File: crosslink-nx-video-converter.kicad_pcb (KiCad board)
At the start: 2 copper layers, 105.7 x 60 mm, 37 parts, among them J1 DC_SOCKET, J2 031-70526-21, J3 031-70526-21, J4 WE_68715014522_ONE-SIDE, J5 WE_68715014522_ONE-SIDE, J6 FTSH-105-01-F-DV-K, J7 FTSH-105-01-L-DV-K, J8 2X05, SW1 SW_DIP_x06, U1 NCV51200MNTXG, U10 GS2971A, U11 LIFCL-40-9BG256C, U12 SC18IS602BIPW, U13 W25Q32JVSSIQ, U2 AP62301WU-7, U3 AP62301WU-7, U4 AP62301WU-7, U5 AP7330-W5-7, U6 AP7330-W5-7, U7 AP7330-W5-7, U8 MT41K128M16JT-125_K, U9 GS2988, Y1 ABM7_27.000MH_D2Y_T, Y2 OSC40M-3.3_S5

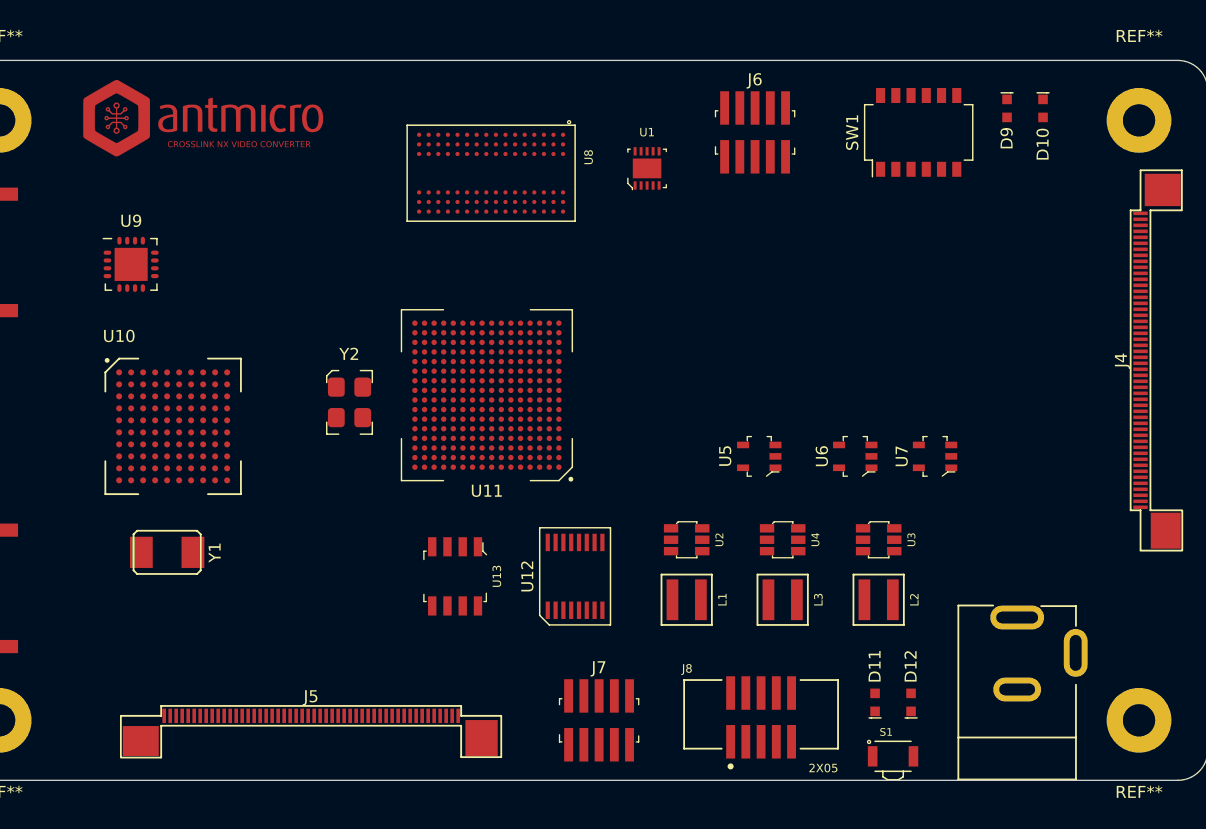
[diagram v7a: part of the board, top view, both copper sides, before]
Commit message: Modified power indicator and connected unused pins
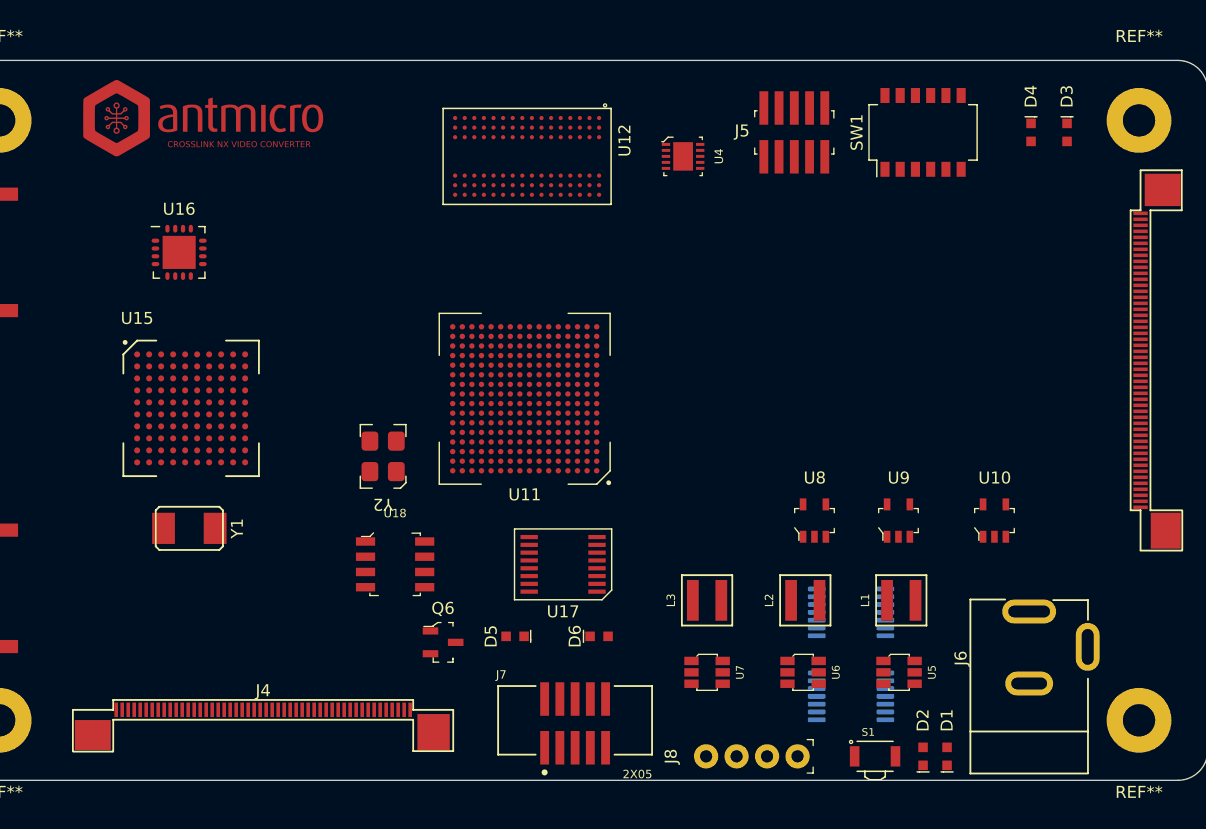
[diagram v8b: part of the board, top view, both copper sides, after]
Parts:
- removed D10, D11, D9: LTST-C190GKT, crosslink-nx-video-converter-footprints:LED_0603
- removed D12: LTST-C190KRKT, crosslink-nx-video-converter-footprints:LED_0603
- removed U1: NCV51200MNTXG, crosslink-nx-video-converter-footprints:DFN-10-1EP_3x3mm
- removed U13: W25Q32JVSSIQ, crosslink-nx-video-converter-footprints:SOIC-8_W5.3mm
- added D1: LTST-C190GKT, crosslink-nx-video-converter-footprints:LED_0603, F.Cu at (159.0, 113.0)
- added D2: LTST-C190GKT, crosslink-nx-video-converter-footprints:LED_0603, F.Cu at (157.0, 113.0)
- added D3: LTST-C190GKT, crosslink-nx-video-converter-footprints:LED_0603, F.Cu at (169.0, 61.0)
- added D4: LTST-C190GKT, crosslink-nx-video-converter-footprints:LED_0603, F.Cu at (166.0, 61.0)
- added D5: LTST-C190GKT, crosslink-nx-video-converter-footprints:LED_0603, F.Cu at (123.0, 103.0)
- added D6: LTST-C190KRKT, crosslink-nx-video-converter-footprints:LED_0603, F.Cu at (130.0, 103.0)
- added Q6: 2N7002, crosslink-nx-video-converter-footprints:SOT-23-3, F.Cu at (117.0, 103.5)
- added U15: GS2971A, crosslink-nx-video-converter-footprints:BGA100_11x11mm, F.Cu at (96.0, 84.0)
- added U16: GS2988, crosslink-nx-video-converter-footprints:QFN-16_EP_4x4_Pitch0.65mm, F.Cu at (95.0, 71.0)
- added U17: SC18IS602BIPW, crosslink-nx-video-converter-footprints:SC18IS602B, F.Cu at (127.0, 97.0)
- added U18: W25Q32JVSSIQ, crosslink-nx-video-converter-footprints:SOIC-8_W5.3mm, F.Cu at (113.0, 97.0)
- J5: value WE_68715014522_ONE-SIDE -> FTSH-105-01-F-DV-K; footprint crosslink-nx-video-converter-footprints:WE_68715014522_ONE-SIDE -> crosslink-nx-video-converter-footprints:PinHeader_2x5_P1.27_SMD
- J6: value FTSH-105-01-F-DV-K -> WE_68715014522_ONE-SIDE; footprint crosslink-nx-video-converter-footprints:PinHeader_2x5_P1.27_SMD -> crosslink-nx-video-converter-footprints:WE_68715014522_ONE-SIDE
- J7: value FTSH-105-01-L-DV-K -> 2X05; footprint crosslink-nx-video-converter-footprints:PinHeader_2x5_P1.27_SMD -> crosslink-nx-video-converter-footprints:SHF-105-01-X-D-SM
- J8: value 2X05 -> 61300411121; footprint crosslink-nx-video-converter-footprints:SHF-105-01-X-D-SM -> antmicro-footprints:PinHeader_1x4_P2.54mm_Drill1.02mm
- U10: value GS2971A -> AP7330-W5-7; footprint crosslink-nx-video-converter-footprints:BGA100_11x11mm -> crosslink-nx-video-converter-footprints:SOT-23-5
- U11: footprint crosslink-nx-video-converter-footprints:BGA-256_16x16_14.0x14.0mm -> antmicro-footprints:BGA-256_16x16_14.0x14.0mm
- U12: value SC18IS602BIPW -> MT41K128M16JT-125_K; footprint crosslink-nx-video-converter-footprints:SC18IS602B -> crosslink-nx-video-converter-footprints:BGA80P96C6X16_800X1400X110
- U2, U3: value AP62301WU-7 -> LM339; footprint crosslink-nx-video-converter-footprints:TSOT23-6 -> antmicro-footprints:TSSOP-14_4.4x5mm_P0.65mm; moved to B.Cu
- U4: value AP62301WU-7 -> NCV51200MNTXG; footprint crosslink-nx-video-converter-footprints:TSOT23-6 -> crosslink-nx-video-converter-footprints:DFN-10-1EP_3x3mm
- U5, U6, U7: value AP7330-W5-7 -> AP62301WU-7; footprint crosslink-nx-video-converter-footprints:SOT-23-5 -> crosslink-nx-video-converter-footprints:TSOT23-6
- U8: value MT41K128M16JT-125_K -> AP7330-W5-7; footprint crosslink-nx-video-converter-footprints:BGA80P96C6X16_800X1400X110 -> crosslink-nx-video-converter-footprints:SOT-23-5
- U9: value GS2988 -> AP7330-W5-7; footprint crosslink-nx-video-converter-footprints:QFN-16_EP_4x4_Pitch0.65mm -> crosslink-nx-video-converter-footprints:SOT-23-5
- moved J4 77.9 mm to (102.0, 108.5), turned to 0 degrees
- moved U10 68.9 mm to (162.9, 93.3)
- moved U9 67.4 mm to (154.9, 93.3)
- moved J5 62.7 mm to (146.3, 61.0), turned to 180 degrees
- moved U8 39.6 mm to (147.9, 93.3), turned to 0 degrees
- moved J6 36.8 mm to (174.5, 80.0), turned to 90 degrees
- moved U12 35.2 mm to (124.0, 63.0), turned to -90 degrees
- moved U4 33.0 mm to (137.0, 63.0)
- moved U7 26.2 mm to (139.0, 106.0), turned to -90 degrees
- moved U5 21.4 mm to (155.0, 106.0), turned to -90 degrees
- moved U6 18.5 mm to (147.0, 106.0), turned to -90 degrees
- moved L1 17.9 mm to (155.2, 100.0), turned to 180 degrees
- moved U2 15.0 mm to (151.0, 101.0), turned to 0 degrees
- moved U3 13.3 mm to (151.0, 108.0), turned to 0 degrees
- moved L3 6.30 mm to (139.0, 100.0), turned to 180 degrees
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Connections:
- net /FPGA/40MHz_3V3 renamed 40MHz_3V3
- net /FPGA/JTAG_EN renamed JTAG_EN
- net /FPGA/TCK renamed TCK
- net /FPGA/TDI renamed TDI
- net /FPGA/TDO renamed TDO
- net /FPGA/TMS renamed TMS
- net FCC1_SCL1 renamed /Peripherals/FCC1_SCL1
- net FCC1_SCL2 renamed /Peripherals/FCC1_SCL2
- net FCC1_SDA1 renamed /Peripherals/FCC1_SDA1
- net FCC1_SDA2 renamed /Peripherals/FCC1_SDA2
- net FFC1_RESET renamed /Peripherals/FFC1_RESET
- net FFC1_VSYNC0 renamed /Peripherals/FFC1_VSYNC0
- net FFC1_VSYNC1 renamed /Peripherals/FFC1_VSYNC1
- net MIPI0_CLK_N renamed /Peripherals/MIPI0_CLK_N
- net MIPI0_CLK_P renamed /Peripherals/MIPI0_CLK_P
- net MIPI0_D0_N renamed /Peripherals/MIPI0_D0_N
- net MIPI0_D0_P renamed /Peripherals/MIPI0_D0_P
- net MIPI0_D1_N renamed /Peripherals/MIPI0_D1_N
- net MIPI0_D1_P renamed /Peripherals/MIPI0_D1_P
- net MIPI0_D2_N renamed /Peripherals/MIPI0_D2_N
- net MIPI0_D2_P renamed /Peripherals/MIPI0_D2_P
- net MIPI0_D3_N renamed /Peripherals/MIPI0_D3_N
- net MIPI0_D3_P renamed /Peripherals/MIPI0_D3_P
- J4 pad 19: MIPI1_D3_N -> /Peripherals/MIPI2_D3_N
- J4 pad 20: MIPI1_D3_P -> /Peripherals/MIPI2_D3_P
- J4 pad 21: MIPI1_D2_N -> /Peripherals/MIPI2_D2_N
- J4 pad 22: MIPI1_D2_P -> /Peripherals/MIPI2_D2_P
- J4 pad 23: MIPI1_D1_N -> /Peripherals/MIPI2_D1_N
- J4 pad 24: MIPI1_D1_P -> /Peripherals/MIPI2_D1_P
- J4 pad 25: MIPI1_D0_N -> /Peripherals/MIPI2_D0_N
- J4 pad 26: MIPI1_D0_P -> /Peripherals/MIPI2_D0_P
- J4 pad 28: MIPI1_CLK_N -> /Peripherals/MIPI2_CLK_N
- J4 pad 29: MIPI1_CLK_P -> /Peripherals/MIPI2_CLK_P
- J5 pad 1: unconnected-(J5-Pad1) -> AUDIO_ACLK
- J5 pad 10: unconnected-(J5-Pad10) -> AUDIO_MCLK
- J5 pad 2: unconnected-(J5-Pad2) -> AUDIO_ACLK
- J5 pad 3: unconnected-(J5-Pad3) -> AUDIO_WCLK
- J5 pad 4: unconnected-(J5-Pad4) -> AUDIO_WCLK
- J5 pad 5: unconnected-(J5-Pad5) -> AUDIO_OUT_CH1_2
- J5 pad 6: unconnected-(J5-Pad6) -> AUDIO_OUT_CH5_6
- J5 pad 7: unconnected-(J5-Pad7) -> AUDIO_OUT_CH3_4
- J5 pad 8: unconnected-(J5-Pad8) -> AUDIO_OUT_CH7_8
- J6 pad 1: AUDIO_ACLK -> unconnected-(J6-Pad1)
- J6 pad 10: AUDIO_MCLK -> unconnected-(J6-Pad10)
- J6 pad 2: AUDIO_ACLK -> unconnected-(J6-Pad2)
- J6 pad 3: AUDIO_WCLK -> unconnected-(J6-Pad3)
- J6 pad 4: AUDIO_WCLK -> unconnected-(J6-Pad4)
- J6 pad 5: AUDIO_OUT_CH1_2 -> unconnected-(J6-Pad5)
- J6 pad 6: AUDIO_OUT_CH5_6 -> unconnected-(J6-Pad6)
- J6 pad 7: AUDIO_OUT_CH3_4 -> unconnected-(J6-Pad7)
- J6 pad 8: AUDIO_OUT_CH7_8 -> unconnected-(J6-Pad8)
- J7 pad 1: unconnected-(J7-Pad1) -> +3V3
- J7 pad 10: GND -> Net-(J7-Pad10)
- J7 pad 2: FCC2_SDA1 -> Net-(J7-Pad2)
- J7 pad 3: /FPGA/SPI_CLK_SOFT -> GND
- J7 pad 4: FCC2_SCL1 -> Net-(J7-Pad4)
- J7 pad 5: /FPGA/MOSI_SOFT -> GND
- J7 pad 6: GND -> Net-(J7-Pad6)
- J7 pad 7: /FPGA/MISO_SOFT -> unconnected-(J7-Pad7)
- J7 pad 8: /FPGA/PROGRAMN_SOFT -> Net-(J7-Pad8)
- J7 pad 9: /FPGA/~{FLASH_CS_SOFT} -> GND
- J8 pad 1: +3V3 -> GND
- J8 pad 2: Net-(J8-Pad2) -> SCL
- J8 pad 3: GND -> SDA
- J8 pad 4: Net-(J8-Pad4) -> GND
- L1 pad 1: Net-(C12-Pad2) -> Net-(C14-Pad2)
- L2 pad 1: Net-(C13-Pad2) -> Net-(C15-Pad2)
- L3 pad 1: Net-(C14-Pad2) -> Net-(C16-Pad2)
- U11 pad A3: MIPI1_D2_P -> /Peripherals/MIPI1_D2_P
- U11 pad A4: MIPI1_D0_P -> /Peripherals/MIPI1_D0_P
- U11 pad A5: MIPI1_CLK_P -> /Peripherals/MIPI1_CLK_P
- U11 pad A6: MIPI1_D1_P -> /Peripherals/MIPI1_D1_P
- U11 pad A7: MIPI1_D3_P -> /Peripherals/MIPI1_D3_P
- U11 pad B3: MIPI1_D2_N -> /Peripherals/MIPI1_D2_N
- U11 pad B4: MIPI1_D0_N -> /Peripherals/MIPI1_D0_N
- U11 pad B5: MIPI1_CLK_N -> /Peripherals/MIPI1_CLK_N
- U11 pad B6: MIPI1_D1_N -> /Peripherals/MIPI1_D1_N
- U11 pad B7: MIPI1_D3_N -> /Peripherals/MIPI1_D3_N
- U11 pad D4: RESET_TRST -> /SDI/RESET_TRST
- U11 pad D5: STANDBY -> /SDI/STANDBY
- U11 pad D6: SW_EN -> /SDI/SW_EN
- U11 pad E10: FFC2_VSYNC1 -> /Peripherals/FFC2_VSYNC1
- U11 pad E13: FCC2_SDA2 -> /Peripherals/FCC2_SDA2
- U11 pad E4: ~{CS_TMS} -> /SDI/~{CS_TMS}
- U11 pad E5: SCLK_TCK -> /SDI/SCLK_TCK
- U11 pad E6: TIM_861 -> /SDI/TIM_861
- U11 pad E9: FFC2_RESET -> /Peripherals/FFC2_RESET
- U11 pad F15: FCC2_SCL2 -> /Peripherals/FCC2_SCL2
- U11 pad F4: SDOUT_TDO -> /SDI/SDOUT_TDO
- U11 pad F6: SDIN_TDI -> /SDI/SDIN_TDI
- U11 pad F9: FFC2_VSYNC0 -> /Peripherals/FFC2_VSYNC0
- U11 pad G10: Net-(R70-Pad1) -> SCL
- U11 pad G3: SDI_STAT5 -> /SDI/SDI_STAT5
- U11 pad G4: ~{SDO_DISABLE} -> /SDI/~{SDO_DISABLE}
- U11 pad G6: SDO_EN/DIS -> /SDI/SDO_EN/DIS
- U11 pad G9: Net-(R69-Pad1) -> SDA
- U11 pad H1: SDI_D4 -> /SDI/SDI_D4
- U11 pad H12: DVB_ASI -> /SDI/DVB_ASI
- U11 pad H2: SDI_D5 -> /SDI/SDI_D5
- U11 pad H3: SDI_D3 -> /SDI/SDI_D3
- U11 pad H4: SDI_D2 -> /SDI/SDI_D2
- U11 pad H5: SDI_D1 -> /SDI/SDI_D1
- U11 pad H6: SDI_D0 -> /SDI/SDI_D0
- U11 pad J1: SDI_D7 -> /SDI/SDI_D7
- U11 pad J11: AUDIO_EN/~{DIS} -> /SDI/AUDIO_EN/~{DIS}
- U11 pad J12: IOPROC_EN/~{DIS} -> /SDI/IOPROC_EN/~{DIS}
- U11 pad J15: 20bit/~{10bit} -> /SDI/20bit/~{10bit}
- U11 pad J16: ~{SMPTE_BYPASS} -> /SDI/~{SMPTE_BYPASS}
- U11 pad J2: SDI_D8 -> /SDI/SDI_D8
- U11 pad J5: SDI_D6 -> /SDI/SDI_D6
- U11 pad J6: SDI_PCLK -> /SDI/SDI_PCLK
- U11 pad K1: SDI_D9 -> /SDI/SDI_D9
- U11 pad K11: JTAG/~{HOST} -> /SDI/JTAG/~{HOST}
- U11 pad K12: ~{RC_BYP} -> /SDI/~{RC_BYP}
- U11 pad K2: SDI_D10 -> /SDI/SDI_D10
- U11 pad K3: SDI_D12 -> /SDI/SDI_D12
- U11 pad K4: SDI_D11 -> /SDI/SDI_D11
- U11 pad K5: SDI_D14 -> /SDI/SDI_D14
- U11 pad K6: SDI_D13 -> /SDI/SDI_D13
- U11 pad K7: MIPI2_D3_N -> /Peripherals/MIPI2_D3_N
- U11 pad L1: SDI_D15 -> /SDI/SDI_D15
- U11 pad L10: DDR3_A8 -> /DDR3/DDR3_A8
- U11 pad L11: DDR3_A7 -> /DDR3/DDR3_A7
- U11 pad L12: DDR3_A10 -> /DDR3/DDR3_A10
- U11 pad L2: SDI_D16 -> /SDI/SDI_D16
- U11 pad L3: SDI_STAT2 -> /SDI/SDI_STAT2
- U11 pad L4: SDI_D19 -> /SDI/SDI_D19
- U11 pad L5: SDI_STAT0 -> /SDI/SDI_STAT0
- U11 pad L6: MIPI2_D3_P -> /Peripherals/MIPI2_D3_P
- U11 pad L7: MIPI2_D2_P -> /Peripherals/MIPI2_D2_P
- U11 pad L8: DDR3_BA2 -> /DDR3/DDR3_BA2
- U11 pad L9: ~{DDR3_RAS} -> /DDR3/~{DDR3_RAS}
- U11 pad M1: SDI_D17 -> /SDI/SDI_D17
- U11 pad M10: DDR3_ODT -> /DDR3/DDR3_ODT
- U11 pad M12: DDR3_A6 -> /DDR3/DDR3_A6
- U11 pad M13: DDR3_A9 -> /DDR3/DDR3_A9
- U11 pad M14: DDR3_A3 -> /DDR3/DDR3_A3
- U11 pad M16: DDR3_A11 -> /DDR3/DDR3_A11
- U11 pad M2: SDI_D18 -> /SDI/SDI_D18
- U11 pad M3: SDI_STAT1 -> /SDI/SDI_STAT1
- U11 pad M4: MIPI2_D1_N -> /Peripherals/MIPI2_D1_N
- U11 pad M7: MIPI2_D2_N -> /Peripherals/MIPI2_D2_N
- U11 pad N1: SDI_STAT4 -> /SDI/SDI_STAT4
- U11 pad N10: ~{DDR3_RESET} -> /DDR3/~{DDR3_RESET}
- U11 pad N13: DDR3_A0 -> /DDR3/DDR3_A0
- U11 pad N15: DDR3_A5 -> /DDR3/DDR3_A5
- U11 pad N16: DDR3_A4 -> /DDR3/DDR3_A4
- U11 pad N2: SDI_STAT3 -> /SDI/SDI_STAT3
- U11 pad N3: MIPI2_D0_N -> /Peripherals/MIPI2_D0_N
- U11 pad N4: MIPI2_D1_P -> /Peripherals/MIPI2_D1_P
- U11 pad N8: ~{DDR3_CAS} -> /DDR3/~{DDR3_CAS}
- U11 pad N9: ~{DDR3_WE} -> /DDR3/~{DDR3_WE}
- U11 pad P1: MIPI2_CLK_P -> /Peripherals/MIPI2_CLK_P
- U11 pad P15: DDR3_A1 -> /DDR3/DDR3_A1
- U11 pad P16: DDR3_A2 -> /DDR3/DDR3_A2
- U11 pad P2: MIPI2_CLK_N -> /Peripherals/MIPI2_CLK_N
- U11 pad P3: MIPI2_D0_P -> /Peripherals/MIPI2_D0_P
- U11 pad P5: DDR3_LDQS_N -> /DDR3/DDR3_LDQS_N
- U11 pad P6: DDR3_BA0 -> /DDR3/DDR3_BA0
- U11 pad P7: DDR3_BA1 -> /DDR3/DDR3_BA1
- U11 pad P8: ~{DDR3_CS} -> /DDR3/~{DDR3_CS}
- U11 pad P9: DDR3_CKE -> /DDR3/DDR3_CKE
- U11 pad R10: DDR3_DQ8 -> /DDR3/DDR3_DQ8
- U11 pad R12: DDR3_UDQS_P -> /DDR3/DDR3_UDQS_P
- U11 pad R13: DDR3_DQ11 -> /DDR3/DDR3_DQ11
- U11 pad R14: DDR3_DQ12 -> /DDR3/DDR3_DQ12
- U11 pad R15: DDR3_UDM -> /DDR3/DDR3_UDM
- U11 pad R16: DDR3_DQ15 -> /DDR3/DDR3_DQ15
- U11 pad R3: DDR3_DQ0 -> /DDR3/DDR3_DQ0
- U11 pad R4: DDR3_DQ3 -> /DDR3/DDR3_DQ3
- U11 pad R5: DDR3_LDQS_P -> /DDR3/DDR3_LDQS_P
- U11 pad R6: DDR3_DQ5 -> /DDR3/DDR3_DQ5
- U11 pad R7: DDR3_DQ7 -> /DDR3/DDR3_DQ7
- U11 pad T10: DDR3_CK_N -> /DDR3/DDR3_CK_N
- U11 pad T11: DDR3_DQ10 -> /DDR3/DDR3_DQ10
- U11 pad T12: DDR3_DQ9 -> /DDR3/DDR3_DQ9
- U11 pad T13: DDR3_UDQS_N -> /DDR3/DDR3_UDQS_N
- U11 pad T14: DDR3_DQ13 -> /DDR3/DDR3_DQ13
- U11 pad T15: DDR3_DQ14 -> /DDR3/DDR3_DQ14
- U11 pad T2: DDR3_LDM -> /DDR3/DDR3_LDM
- U11 pad T3: DDR3_DQ1 -> /DDR3/DDR3_DQ1
- U11 pad T4: DDR3_DQ2 -> /DDR3/DDR3_DQ2
- U11 pad T5: DDR3_DQ4 -> /DDR3/DDR3_DQ4
- U11 pad T6: DDR3_DQ6 -> /DDR3/DDR3_DQ6
- U11 pad T7: DDR3_A12 -> /DDR3/DDR3_A12
- U11 pad T8: DDR3_A13 -> /DDR3/DDR3_A13
- U11 pad T9: DDR3_CK_P -> /DDR3/DDR3_CK_P
- U2 pad 1: GND -> Net-(D1-Pad1)
- U2 pad 2: Net-(C12-Pad2) -> Net-(D1-Pad1)
- U2 pad 3: Net-(C9-Pad1) -> +5V
- U2 pad 4: Net-(R26-Pad2) (its old number) -> +3V3
- U2 pad 5: Net-(TP11-Pad1) (its old number) -> /Power Supply/VREF_0V45
- U2 pad 6: Net-(C12-Pad1) (its old number) -> 1V0_Power
- U3 pad 1: GND -> Net-(D1-Pad1)
- U3 pad 2: Net-(C13-Pad2) -> Net-(D1-Pad1)
- U3 pad 3: Net-(C10-Pad1) -> +5V
- U3 pad 4: Net-(R28-Pad1) -> +1V35
- U3 pad 5: Net-(TP12-Pad1) (its old number) -> /Power Supply/VREF_0V45
- U3 pad 6: Net-(C13-Pad1) (its old number) -> +1V2
- U4 pad 1: GND -> Net-(C4-Pad2)
- U4 pad 2: Net-(C14-Pad2) -> Net-(C3-Pad1)
- U4 pad 3: Net-(C11-Pad1) (its old number) -> Vtt
- U4 pad 4: Net-(R30-Pad2) -> GND
- U4 pad 5: Net-(TP13-Pad1) -> Vtt
- U4 pad 6: Net-(C14-Pad1) -> Vref
- U5 pad 1: Net-(R23-Pad2) -> GND
- U5 pad 2: GND -> Net-(C14-Pad2)
- U6 pad 1: Net-(R24-Pad2) -> GND
- U6 pad 2: GND -> Net-(C15-Pad2)
- U7 pad 1: Net-(R25-Pad2) -> GND
- U7 pad 2: GND -> Net-(C16-Pad2)
- U9 pad 1: /SDI/SDO_P -> Net-(R20-Pad2)
- U9 pad 2: /SDI/SDO_N -> GND
- U9 pad 3: GND -> Net-(R29-Pad2)
- U9 pad 5: unconnected-(U9-Pad5) -> Net-(R33-Pad1)
